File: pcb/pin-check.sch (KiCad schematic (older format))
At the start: 55 parts, among them J1 AVR-ISP-6, P1 USB_C_Receptacle_USB2.0, SW1 SW_Push, SW2 SW_Push, SW3 SW_Push, SW4 SW_Push, SW5 SW_Push, SW6 SW_Push, SW7 Reset, SW8 Boot, U1 ATmega328P-PU, Y1 16MHz

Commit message: smaller!
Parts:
- removed D5, D6: 1N4148, pin-check:D_DO-35_SOD27_P5.08mm_Horizontal, symbol Device:D
- removed D9: LED, LED_THT:LED_D3.0mm, symbol Device:LED
- removed R7: 1.5k, Resistor_THT:R_Axial_DIN0204_L3.6mm_D1.6mm_P7.62mm_Horizontal, symbol Device:R
- removed SW5, SW6: SW_Push, Button_Switch_Keyboard:SW_Cherry_MX_1.00u_PCB, symbol Switch:SW_Push
- J1: footprint Connector_PinHeader_2.54mm:PinHeader_2x03_P2.54mm_Horizontal -> Connector_PinHeader_2.54mm:PinHeader_2x03_P2.54mm_Vertical
- renumbered H17 to H10, H12 to H11, H7 to H12, H6 to H13, H11 to H14, H10 to H15, H9 to H16, H8 to H17, H13 to H6, H14 to H7, H15 to H8, H16 to H9
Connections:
- net Col4 renamed C3
- net Col5 renamed C4
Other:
- note removed: "Power LED"
- moved on the sheet: D1, D2, D3, D4, H1, H10, H11, H12, H13, H14, H15, H16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

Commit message: symbols for trrs
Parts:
- added J2: SJ-43514, pin-check:CUI_SJ-43514, symbol pin-check:SJ-43514
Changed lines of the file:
@@
 Text Label 5100 6100 2    50   ~ 0
 C4
+$Comp
+L pin-check:SJ-43514 J2
+U 1 1 5F1976DA
+P 3700 4600
+F 0 "J2" H 3757 5067 50  0000 C CNN
+F 1 "SJ-43514" H 3757 4976 50  0000 C CNN
+F 2 "pin-check:CUI_SJ-43514" H 3700 4600 50  0001 L BNN
+F 3 "1.04" H 3700 4600 50  0001 L BNN
+F 4 "CUI INC" H 3700 4600 50  0001 L BNN "Field4"
+F 5 "MANUFACTURER RECOMMENDATIONS" H 3700 4600 50  0001 L BNN "Field5"
+	1    3700 4600
+	1    0    0    -1
+$EndComp
 $EndSCHEMATC

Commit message: new version
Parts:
- added R7, R8: 4.7k, Resistor_THT:R_Axial_DIN0204_L3.6mm_D1.6mm_P7.62mm_Horizontal, symbol Device:R
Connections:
- net +5V: now also J2.4, R7.1, R8.1
- net C4: now also J2.3, R8.2
- net C5: now also J2.2, R7.2
- net GND: now also J2.1
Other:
- note added: "TRRS Jack"
- moved on the sheet: D1, D2, D3, D4, H1, H10, H11, H12, H13, H14, H15, H16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

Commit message: v1.0.1
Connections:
- net Col0 renamed ColA
- net Col1 renamed ColB
- net Col2 renamed ColC
- net Col3 renamed ColD
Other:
- moved on the sheet: H14, H15, H16, H17
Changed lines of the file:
@@
 Title "pin-check"
 Date ""
-Rev "v1.0.0"
+Rev "v1.0.1"
 Comp ""
 Comment1 ""
@@
 Row0
 Text Label 2650 3100 0    50   ~ 0
-Col1
+ColB
 $Comp
 L Mechanical:MountingHole_Pad H1
@@
 	2650 2900 3050 2900
 Text Label 3900 6000 2    50   ~ 0
-Col0Ext
+ColAExt
 Text Label 3150 6000 2    50   ~ 0
 Row0Ext
 Connection ~ 7100 4900
 Text Label 6600 5000 3    50   ~ 0
-Col0Ext
+ColAExt
 Wire Wire Line
 	6500 4900 7100 4900
@@
 $EndComp
 Text Label 2650 3200 0    50   ~ 0
-Col2
+ColC
 Text Label 2650 3300 0    50   ~ 0
-Col3
+ColD
 $Comp
 L Switch:SW_Push SW2
@@
 Connection ~ 9350 4600
 Text Label 7550 5000 3    50   ~ 0
-Col1Ext
+ColBExt
 Text Label 8450 5000 3    50   ~ 0
-Col2Ext
+ColCExt
 Text Label 9350 5000 3    50   ~ 0
-Col3Ext
+ColDExt
 $Comp
 L Mechanical:MountingHole_Pad H3
@@
 $EndComp
 Text Label 3900 6200 2    50   ~ 0
-Col1Ext
+ColBExt
 Text Label 3900 6400 2    50   ~ 0
-Col2Ext
+ColCExt
 Text Label 3900 6600 2    50   ~ 0
-Col3Ext
+ColDExt
 Text Label 8450 4200 1    50   ~ 0
-Col2
+ColC
 Text Label 9350 4200 1    50   ~ 0
-Col3
+ColD
 $Comp
 L Mechanical:MountingHole_Pad H17
 U 1 1 5F25327F
+P 5800 6600
+F 0 "H17" V 5754 6750 50  0000 L CNN
+F 1 "Pad" V 5845 6750 50  0000 L CNN
+F 2 "Connector_Wire:SolderWire-0.5sqmm_1x01_D0.9mm_OD2.1mm" H 5800 6600 50  0001 C CNN
+F 3 "~" H 5800 6600 50  0001 C CNN
+	1    5800 6600
+	0    1    1    0
+$EndComp
+$Comp
+L Mechanical:MountingHole_Pad H16
+U 1 1 5F25363B
+P 5800 6400
+F 0 "H16" V 5754 6550 50  0000 L CNN
+F 1 "Pad" V 5845 6550 50  0000 L CNN
+F 2 "Connector_Wire:SolderWire-0.5sqmm_1x01_D0.9mm_OD2.1mm" H 5800 6400 50  0001 C CNN
+F 3 "~" H 5800 6400 50  0001 C CNN
+	1    5800 6400
+	0    1    1    0
+$EndComp
+$Comp
+L Mechanical:MountingHole_Pad H15
+U 1 1 5F253939
+P 5800 6200
+F 0 "H15" V 5754 6350 50  0000 L CNN
+F 1 "Pad" V 5845 6350 50  0000 L CNN
+F 2 "Connector_Wire:SolderWire-0.5sqmm_1x01_D0.9mm_OD2.1mm" H 5800 6200 50  0001 C CNN
+F 3 "~" H 5800 6200 50  0001 C CNN
+	1    5800 6200
+	0    1    1    0
+$EndComp
+$Comp
+L Mechanical:MountingHole_Pad H14
+U 1 1 5F253BB2
 P 5800 6000
-F 0 "H17" V 5754 6150 50  0000 L CNN
+F 0 "H14" V 5754 6150 50  0000 L CNN
 F 1 "Pad" V 5845 6150 50  0000 L CNN
 F 2 "Connector_Wire:SolderWire-0.5sqmm_1x01_D0.9mm_OD2.1mm" H 5800 6000 50  0001 C CNN
@@
 	0    1    1    0
 $EndComp
-$Comp
-L Mechanical:MountingHole_Pad H16
-U 1 1 5F25363B
-P 5800 6200
-F 0 "H16" V 5754 6350 50  0000 L CNN
-F 1 "Pad" V 5845 6350 50  0000 L CNN
-F 2 "Connector_Wire:SolderWire-0.5sqmm_1x01_D0.9mm_OD2.1mm" H 5800 6200 50  0001 C CNN
-F 3 "~" H 5800 6200 50  0001 C CNN
-	1    5800 6200
-	0    1    1    0
-$EndComp
-$Comp
-L Mechanical:MountingHole_Pad H15
-U 1 1 5F253939
-P 5800 6400
-F 0 "H15" V 5754 6550 50  0000 L CNN
-F 1 "Pad" V 5845 6550 50  0000 L CNN
-F 2 "Connector_Wire:SolderWire-0.5sqmm_1x01_D0.9mm_OD2.1mm" H 5800 6400 50  0001 C CNN
-F 3 "~" H 5800 6400 50  0001 C CNN
-	1    5800 6400
-	0    1    1    0
-$EndComp
-$Comp
-L Mechanical:MountingHole_Pad H14
-U 1 1 5F253BB2
-P 5800 6600
-F 0 "H14" V 5754 6750 50  0000 L CNN
-F 1 "Pad" V 5845 6750 50  0000 L CNN
-F 2 "Connector_Wire:SolderWire-0.5sqmm_1x01_D0.9mm_OD2.1mm" H 5800 6600 50  0001 C CNN
-F 3 "~" H 5800 6600 50  0001 C CNN
-	1    5800 6600
-	0    1    1    0
-$EndComp
+Text Label 5700 6600 2    50   ~ 0
+B1
+Text Label 5700 6400 2    50   ~ 0
+B2
+Text Label 5700 6200 2    50   ~ 0
+B3
 Text Label 5700 6000 2    50   ~ 0
-B1
-Text Label 5700 6200 2    50   ~ 0
-B2
-Text Label 5700 6400 2    50   ~ 0
-B3
-Text Label 5700 6600 2    50   ~ 0
 B4
 $Comp
@@
 B4
 Text Label 2650 2700 0    50   ~ 0
-Col0
+ColA
 Text Label 2650 3600 0    50   ~ 0
 C5
@@
 $EndComp
 Text Label 7550 4200 1    50   ~ 0
-Col1
+ColB
 Text Label 6600 4200 1    50   ~ 0
-Col0
+ColA
 $Comp
 L power:GND #PWR05

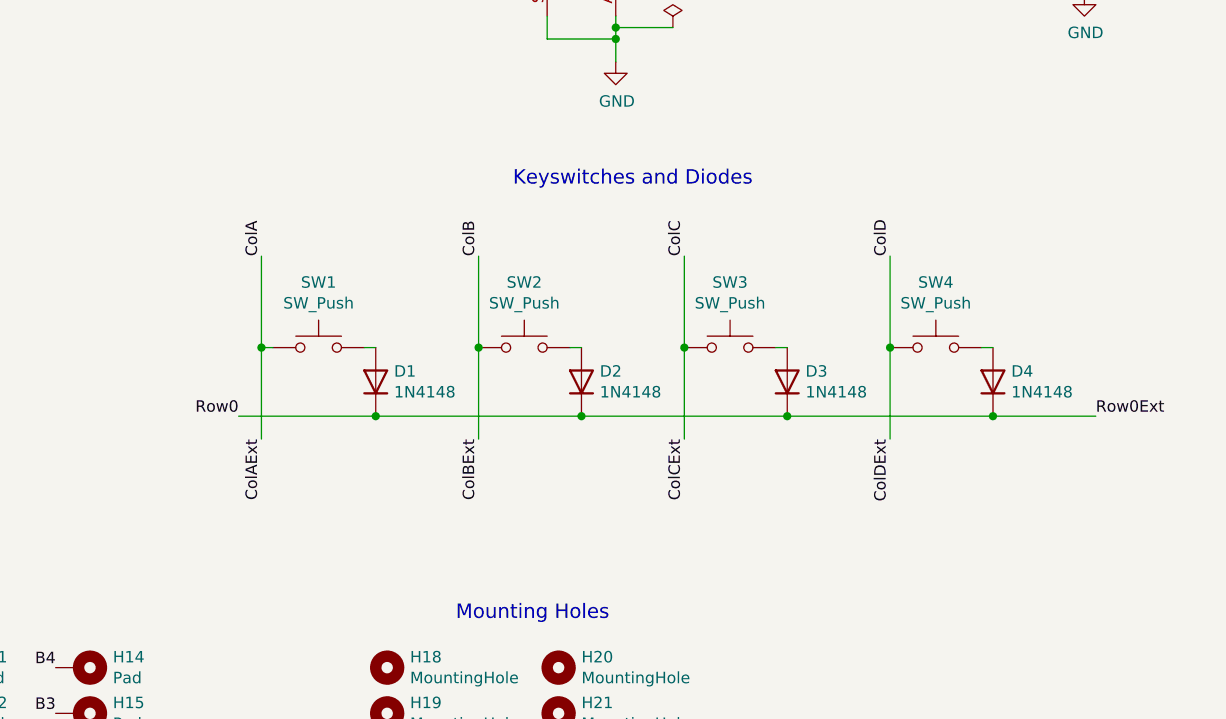
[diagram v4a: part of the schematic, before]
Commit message: Update README, add hybrid MX/ALPS switch footprints
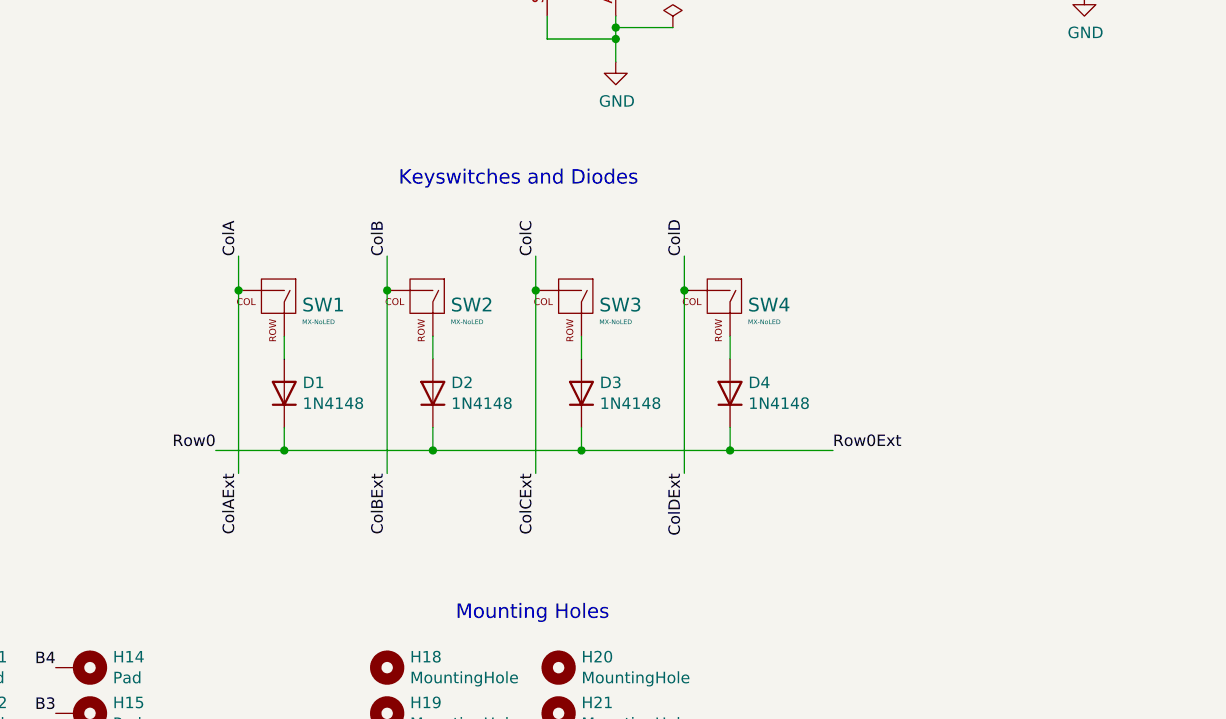
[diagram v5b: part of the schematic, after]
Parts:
- removed SW1, SW2, SW3, SW4: SW_Push, Button_Switch_Keyboard:SW_Cherry_MX_1.00u_PCB, symbol Switch:SW_Push
- added SW1, SW2, SW3, SW4: MX-NoLED, pin-check:MX-1U-NoLED, symbol pin-check:MX-NoLED
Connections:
- net ColA: now also SW1.2 (ROW)
- net ColB: now also SW2.2 (ROW)
- net ColC: now also SW3.2 (ROW)
- net ColD: now also SW4.2 (ROW)
- net at D1.2 (A): now also SW1.1 (COL)
- net at D2.2 (A): now also SW2.1 (COL)
- net at D3.2 (A): now also SW3.1 (COL)
- net at D4.2 (A): now also SW4.1 (COL)
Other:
- moved on the sheet: D1, D2, D3, D4
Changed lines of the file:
@@
 Title "pin-check"
 Date ""
-Rev "v1.0.1"
+Rev "v1.1.0"
 Comp ""
 Comment1 ""
@@
 $EndComp
 $Comp
-L power:GND #PWR06
-U 1 1 5F169047
-P 8150 3350
-F 0 "#PWR06" H 8150 3100 50  0001 C CNN
-F 1 "GND" H 8155 3177 50  0000 C CNN
-F 2 "" H 8150 3350 50  0001 C CNN
-F 3 "" H 8150 3350 50  0001 C CNN
-	1    8150 3350
-	1    0    0    -1
-$EndComp
-$Comp
 L Device:R R4
 U 1 1 5F16FEDB
@@
 Text Label 3150 6000 2    50   ~ 0
 Row0Ext
-Connection ~ 7100 4900
-Text Label 6600 5000 3    50   ~ 0
-ColAExt
-Wire Wire Line
-	6500 4900 7100 4900
-Wire Wire Line
-	6650 4600 6600 4600
-Wire Wire Line
-	7050 4600 7100 4600
-Text Label 6500 4900 2    50   ~ 0
-Row0
-$Comp
-L Device:D D1
-U 1 1 5F10EEDE
-P 7100 4750
-F 0 "D1" V 7146 4670 50  0000 R CNN
-F 1 "1N4148" V 7055 4670 50  0000 R CNN
-F 2 "pin-check:D_DO-35_SOD27_P5.08mm_Horizontal" H 7100 4750 50  0001 C CNN
-F 3 "~" H 7100 4750 50  0001 C CNN
-	1    7100 4750
-	0    -1   -1   0
-$EndComp
-$Comp
-L Switch:SW_Push SW1
-U 1 1 5F10BCBB
-P 6850 4600
-F 0 "SW1" H 6850 4885 50  0000 C CNN
-F 1 "SW_Push" H 6850 4794 50  0000 C CNN
-F 2 "Button_Switch_Keyboard:SW_Cherry_MX_1.00u_PCB" H 6850 4800 50  0001 C CNN
-F 3 "~" H 6850 4800 50  0001 C CNN
-	1    6850 4600
-	1    0    0    -1
-$EndComp
 Text Label 2650 3200 0    50   ~ 0
 ColC
 Text Label 2650 3300 0    50   ~ 0
 ColD
-$Comp
-L Switch:SW_Push SW2
-U 1 1 5F1B9489
-P 7750 4600
-F 0 "SW2" H 7750 4885 50  0000 C CNN
-F 1 "SW_Push" H 7750 4794 50  0000 C CNN
-F 2 "Button_Switch_Keyboard:SW_Cherry_MX_1.00u_PCB" H 7750 4800 50  0001 C CNN
-F 3 "~" H 7750 4800 50  0001 C CNN
-	1    7750 4600
-	1    0    0    -1
-$EndComp
-$Comp
-L Device:D D2
-U 1 1 5F1BA8D5
-P 8000 4750
-F 0 "D2" V 8046 4670 50  0000 R CNN
-F 1 "1N4148" V 7955 4670 50  0000 R CNN
-F 2 "pin-check:D_DO-35_SOD27_P5.08mm_Horizontal" H 8000 4750 50  0001 C CNN
-F 3 "~" H 8000 4750 50  0001 C CNN
-	1    8000 4750
-	0    -1   -1   0
-$EndComp
-Wire Wire Line
-	7100 4900 8000 4900
-Connection ~ 8000 4900
-$Comp
-L Switch:SW_Push SW3
-U 1 1 5F1BD5A3
-P 8650 4600
-F 0 "SW3" H 8650 4885 50  0000 C CNN
-F 1 "SW_Push" H 8650 4794 50  0000 C CNN
-F 2 "Button_Switch_Keyboard:SW_Cherry_MX_1.00u_PCB" H 8650 4800 50  0001 C CNN
-F 3 "~" H 8650 4800 50  0001 C CNN
-	1    8650 4600
-	1    0    0    -1
-$EndComp
-$Comp
-L Device:D D3
-U 1 1 5F1C1E03
-P 8900 4750
-F 0 "D3" V 8946 4670 50  0000 R CNN
-F 1 "1N4148" V 8855 4670 50  0000 R CNN
-F 2 "pin-check:D_DO-35_SOD27_P5.08mm_Horizontal" H 8900 4750 50  0001 C CNN
-F 3 "~" H 8900 4750 50  0001 C CNN
-	1    8900 4750
-	0    -1   -1   0
-$EndComp
-$Comp
-L Switch:SW_Push SW4
-U 1 1 5F1C23FE
-P 9550 4600
-F 0 "SW4" H 9550 4885 50  0000 C CNN
-F 1 "SW_Push" H 9550 4794 50  0000 C CNN
-F 2 "Button_Switch_Keyboard:SW_Cherry_MX_1.00u_PCB" H 9550 4800 50  0001 C CNN
-F 3 "~" H 9550 4800 50  0001 C CNN
-	1    9550 4600
-	1    0    0    -1
-$EndComp
-$Comp
-L Device:D D4
-U 1 1 5F1C2FB9
-P 9800 4750
-F 0 "D4" V 9846 4670 50  0000 R CNN
-F 1 "1N4148" V 9755 4670 50  0000 R CNN
-F 2 "pin-check:D_DO-35_SOD27_P5.08mm_Horizontal" H 9800 4750 50  0001 C CNN
-F 3 "~" H 9800 4750 50  0001 C CNN
-	1    9800 4750
-	0    -1   -1   0
-$EndComp
-Wire Wire Line
-	8000 4900 8900 4900
-Connection ~ 8900 4900
-Wire Wire Line
-	8900 4900 9800 4900
-Text Label 10250 4900 0    50   ~ 0
-Row0Ext
-Wire Wire Line
-	6600 4600 6600 5000
-Wire Wire Line
-	7950 4600 8000 4600
-Wire Wire Line
-	8850 4600 8900 4600
-Wire Wire Line
-	9750 4600 9800 4600
-Wire Wire Line
-	6600 4600 6600 4200
-Connection ~ 6600 4600
-Wire Wire Line
-	7550 4600 7550 4200
-Wire Wire Line
-	7550 4600 7550 5000
-Connection ~ 7550 4600
-Wire Wire Line
-	8450 4600 8450 4200
-Wire Wire Line
-	8450 4600 8450 5000
-Connection ~ 8450 4600
-Wire Wire Line
-	9350 4600 9350 4200
-Wire Wire Line
-	9350 4600 9350 5000
-Connection ~ 9350 4600
-Text Label 7550 5000 3    50   ~ 0
-ColBExt
-Text Label 8450 5000 3    50   ~ 0
-ColCExt
-Text Label 9350 5000 3    50   ~ 0
-ColDExt
 $Comp
 L Mechanical:MountingHole_Pad H3
@@
 Text Label 3900 6600 2    50   ~ 0
 ColDExt
-Text Label 8450 4200 1    50   ~ 0
-ColC
-Text Label 9350 4200 1    50   ~ 0
-ColD
 $Comp
 L Mechanical:MountingHole_Pad H17
@@
 	1    0    0    -1
 $EndComp
-Text Label 7550 4200 1    50   ~ 0
-ColB
-Text Label 6600 4200 1    50   ~ 0
-ColA
 $Comp
 L power:GND #PWR05
@@
 Text Notes 7950 1200 0    63   ~ 0
 USB Port
-Text Notes 7700 3900 0    63   ~ 0
-Keyswitches and Diodes
 Text Notes 3450 5800 0    63   ~ 0
 Solder Pads For Additional Rows and Columns
@@
 Text Notes 7450 5800 0    63   ~ 0
 Mounting Holes
-Wire Wire Line
-	9800 4900 10250 4900
-Connection ~ 9800 4900
 Text Label 2650 3400 0    50   ~ 0
 C3
@@
 Text Notes 4200 3900 0    63   ~ 0
 TRRS Jack
+$Comp
+L power:GND #PWR06
+U 1 1 5F169047
+P 8150 3350
+F 0 "#PWR06" H 8150 3100 50  0001 C CNN
+F 1 "GND" H 8155 3177 50  0000 C CNN
+F 2 "" H 8150 3350 50  0001 C CNN
+F 3 "" H 8150 3350 50  0001 C CNN
+	1    8150 3350
+	1    0    0    -1
+$EndComp
+Text Notes 7200 3900 0    63   ~ 0
+Keyswitches and Diodes
+Text Label 6500 4200 1    50   ~ 0
+ColA
+Text Label 7150 4200 1    50   ~ 0
+ColB
+Text Label 8450 4200 1    50   ~ 0
+ColD
+Text Label 7800 4200 1    50   ~ 0
+ColC
+$Comp
+L Device:D D4
+U 1 1 5F1C2FB9
+P 8650 4800
+F 0 "D4" V 8696 4720 50  0000 R CNN
+F 1 "1N4148" V 8605 4720 50  0000 R CNN
+F 2 "pin-check:D_DO-35_SOD27_P5.08mm_Horizontal" H 8650 4800 50  0001 C CNN
+F 3 "~" H 8650 4800 50  0001 C CNN
+	1    8650 4800
+	0    -1   -1   0
+$EndComp
+$Comp
+L Device:D D3
+U 1 1 5F1C1E03
+P 8000 4800
+F 0 "D3" V 8046 4720 50  0000 R CNN
+F 1 "1N4148" V 7955 4720 50  0000 R CNN
+F 2 "pin-check:D_DO-35_SOD27_P5.08mm_Horizontal" H 8000 4800 50  0001 C CNN
+F 3 "~" H 8000 4800 50  0001 C CNN
+	1    8000 4800
+	0    -1   -1   0
+$EndComp
+$Comp
+L Device:D D2
+U 1 1 5F1BA8D5
+P 7350 4800
+F 0 "D2" V 7396 4720 50  0000 R CNN
+F 1 "1N4148" V 7305 4720 50  0000 R CNN
+F 2 "pin-check:D_DO-35_SOD27_P5.08mm_Horizontal" H 7350 4800 50  0001 C CNN
+F 3 "~" H 7350 4800 50  0001 C CNN
+	1    7350 4800
+	0    -1   -1   0
+$EndComp
+$Comp
+L Device:D D1
+U 1 1 5F10EEDE
+P 6700 4800
+F 0 "D1" V 6746 4720 50  0000 R CNN
+F 1 "1N4148" V 6655 4720 50  0000 R CNN
+F 2 "pin-check:D_DO-35_SOD27_P5.08mm_Horizontal" H 6700 4800 50  0001 C CNN
+F 3 "~" H 6700 4800 50  0001 C CNN
+	1    6700 4800
+	0    -1   -1   0
+$EndComp
+$Comp
+L pin-check:MX-NoLED SW1
+U 1 1 5F2FF1B6
+P 6650 4400
+F 0 "SW1" V 6664 4528 60  0000 L CNN
+F 1 "MX-NoLED" V 6738 4528 20  0000 L CNN
+F 2 "pin-check:MX-1U-NoLED" H 6025 4375 60  0001 C CNN
+F 3 "" H 6025 4375 60  0001 C CNN
+	1    6650 4400
+	0    1    1    0
+$EndComp
+Wire Wire Line
+	6700 4550 6700 4650
+$Comp
+L pin-check:MX-NoLED SW2
+U 1 1 5F309D39
+P 7300 4400
+F 0 "SW2" V 7314 4528 60  0000 L CNN
+F 1 "MX-NoLED" V 7388 4528 20  0000 L CNN
+F 2 "pin-check:MX-1U-NoLED" H 6675 4375 60  0001 C CNN
+F 3 "" H 6675 4375 60  0001 C CNN
+	1    7300 4400
+	0    1    1    0
+$EndComp
+$Comp
+L pin-check:MX-NoLED SW3
+U 1 1 5F30C3B9
+P 7950 4400
+F 0 "SW3" V 7964 4528 60  0000 L CNN
+F 1 "MX-NoLED" V 8038 4528 20  0000 L CNN
+F 2 "pin-check:MX-1U-NoLED" H 7325 4375 60  0001 C CNN
+F 3 "" H 7325 4375 60  0001 C CNN
+	1    7950 4400
+	0    1    1    0
+$EndComp
+Wire Wire Line
+	7350 4550 7350 4650
+Wire Wire Line
+	8000 4550 8000 4650
+Wire Wire Line
+	8650 4550 8650 4650
+Wire Wire Line
+	6700 4950 6700 5050
+Wire Wire Line
+	6700 5050 7350 5050
+Wire Wire Line
+	7350 4950 7350 5050
+Connection ~ 7350 5050
+Wire Wire Line
+	7350 5050 8000 5050
+Wire Wire Line
+	8000 4950 8000 5050
+Connection ~ 8000 5050
+Wire Wire Line
+	8000 5050 8650 5050
+Wire Wire Line
+	8650 4950 8650 5050
+Connection ~ 8650 5050
+Wire Wire Line
+	8650 5050 9100 5050
+Text Label 6400 5050 2    50   ~ 0
+Row0
+Text Label 9100 5050 0    50   ~ 0
+Row0Ext
+$Comp
+L pin-check:MX-NoLED SW4
+U 1 1 5F30D201
+P 8600 4400
+F 0 "SW4" V 8614 4528 60  0000 L CNN
+F 1 "MX-NoLED" V 8688 4528 20  0000 L CNN
+F 2 "pin-check:MX-1U-NoLED" H 7975 4375 60  0001 C CNN
+F 3 "" H 7975 4375 60  0001 C CNN
+	1    8600 4400
+	0    1    1    0
+$EndComp
+Wire Wire Line
+	8450 4350 8450 5150
+Wire Wire Line
+	7800 4350 7800 5150
+Wire Wire Line
+	7150 4350 7150 5150
+Wire Wire Line
+	6400 5050 6700 5050
+Connection ~ 6700 5050
+Wire Wire Line
+	6500 4350 6500 5150
+Text Label 6500 5150 3    50   ~ 0
+ColAExt
+Text Label 7150 5150 3    50   ~ 0
+ColBExt
+Text Label 7800 5150 3    50   ~ 0
+ColCExt
+Text Label 8450 5150 3    50   ~ 0
+ColDExt
+Wire Wire Line
+	6500 4350 6500 4200
+Connection ~ 6500 4350
+Wire Wire Line
+	7150 4350 7150 4200
+Connection ~ 7150 4350
+Wire Wire Line
+	7800 4350 7800 4200
+Connection ~ 7800 4350
+Wire Wire Line
+	8450 4350 8450 4200
+Connection ~ 8450 4350
 $EndSCHEMATC

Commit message: also probably not
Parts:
- added U2: MCP23008-xP, Package_DIP:DIP-18_W7.62mm, symbol Interface_Expansion:MCP23008-xP
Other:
- moved on the sheet: D1, D2, D3, D4, H1, H10, H11, H12, H13, H14, H15, H16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
